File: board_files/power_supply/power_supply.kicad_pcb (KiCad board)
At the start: 2 copper layers, 39 parts, among them J1 Screw_Terminal_01x02, J10 Screw_Terminal_01x02, J11 Screw_Terminal_01x02, J12 Screw_Terminal_01x02, J13 Screw_Terminal_01x02, J14 Screw_Terminal_01x02, J15 Screw_Terminal_01x02, J16 Screw_Terminal_01x02, J17 Screw_Terminal_01x02, J2 Screw_Terminal_01x02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

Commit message: Started PSU layout + panel
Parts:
- moved J3 71.8 mm to (30.5, 73.0)
- moved J2 65.9 mm to (30.5, 54.0)
- moved J4 62.8 mm to (30.5, 92.1)
- moved J1 57.4 mm to (30.5, 34.9)
- moved C1 49.8 mm to (107.7, -15.2)
- moved C10 49.8 mm to (69.3, 9.71)
- moved C2 49.8 mm to (61.8, -23.1)
- moved C3 49.8 mm to (28.2, -8.65)
- moved C4 49.8 mm to (42.6, -8.65)
- moved C5 49.8 mm to (28.2, 5.40)
- moved C6 49.8 mm to (61.8, -9.06)
- moved C7 49.8 mm to (42.6, 5.40)
- moved C8 49.8 mm to (76.2, -23.1)
- moved C9 49.8 mm to (57.0, 4.99)
- moved D2 49.8 mm to (27.7, -19.2)
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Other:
- board outline added: 76.2 x 76.2 mm

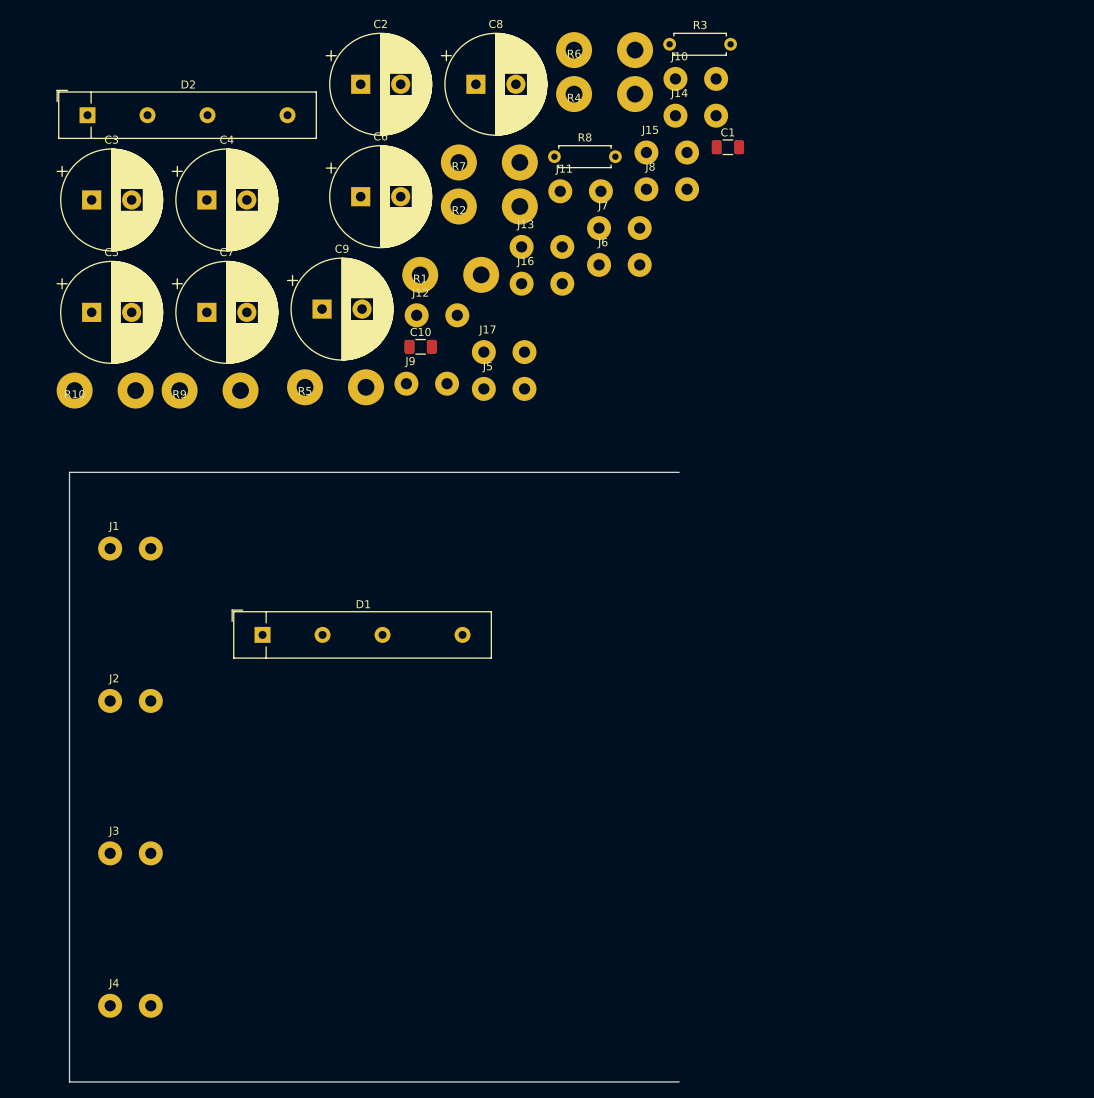
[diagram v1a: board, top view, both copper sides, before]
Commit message: rough component placement
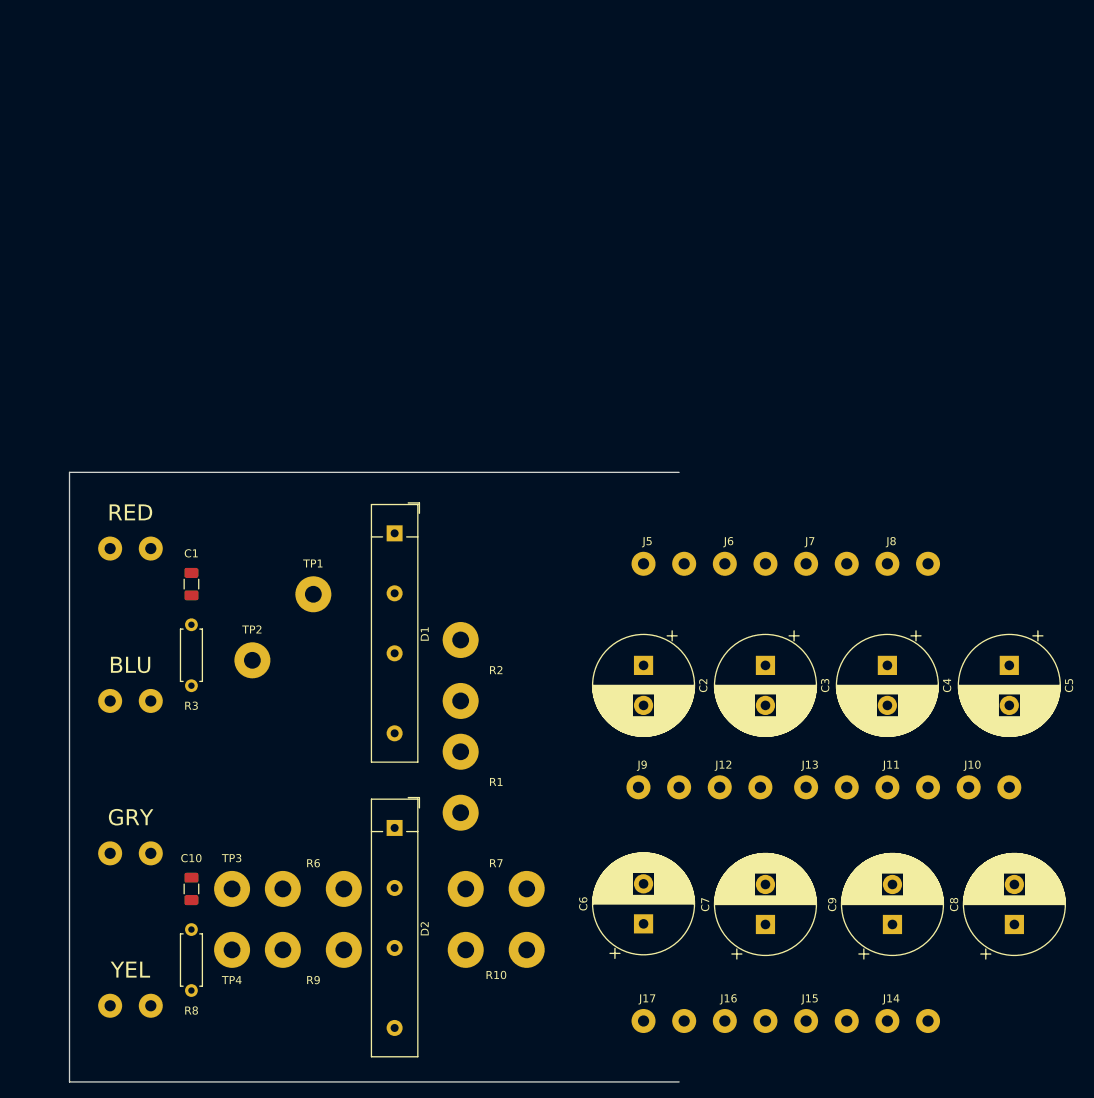
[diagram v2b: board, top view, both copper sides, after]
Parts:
- removed R4, R5: 0, power_supply:12_Gauge_Jumper
- added TP1: TestPoint, power_supply:12_Gauge_Jumper_one_pad, F.Cu at (55.9, 40.6)
- added TP2: TestPoint, power_supply:12_Gauge_Jumper_one_pad, F.Cu at (48.3, 48.9)
- added TP3: TestPoint, power_supply:12_Gauge_Jumper_one_pad, F.Cu at (45.7, 77.5)
- added TP4: TestPoint, power_supply:12_Gauge_Jumper_one_pad, F.Cu at (45.7, 85.1)
- moved C8 124.7 mm to (143.5, 81.9), turned to 90 degrees
- moved C5 122.9 mm to (142.9, 49.5), turned to 270 degrees
- moved J14 116.2 mm to (127.6, 94.0)
- moved R6 111.0 mm to (52.1, 77.5)
- moved J15 110.4 mm to (117.5, 94.0)
- moved R8 106.7 mm to (40.6, 82.5), turned to 270 degrees
- moved C9 104.9 mm to (128.3, 81.9), turned to 90 degrees
- moved C7 103.6 mm to (112.4, 81.9), turned to 90 degrees
- moved C4 103.1 mm to (127.6, 49.5), turned to 270 degrees
- moved C3 102.4 mm to (112.4, 49.5), turned to 270 degrees
- moved C6 97.5 mm to (97.2, 81.8), turned to 90 degrees
- moved D2 97.0 mm to (66.0, 69.8), turned to 270 degrees
- moved J10 95.8 mm to (137.8, 64.8)
- moved J16 95.6 mm to (107.3, 94.0)
- moved R3 94.0 mm to (40.6, 44.5), turned to 270 degrees
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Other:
- board text added: "BLU"
- board text added: "GRY"
- board text added: "RED"
- board text added: "YEL"
